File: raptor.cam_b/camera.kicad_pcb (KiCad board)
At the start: 2 copper layers, 25 x 26 mm, 7 parts

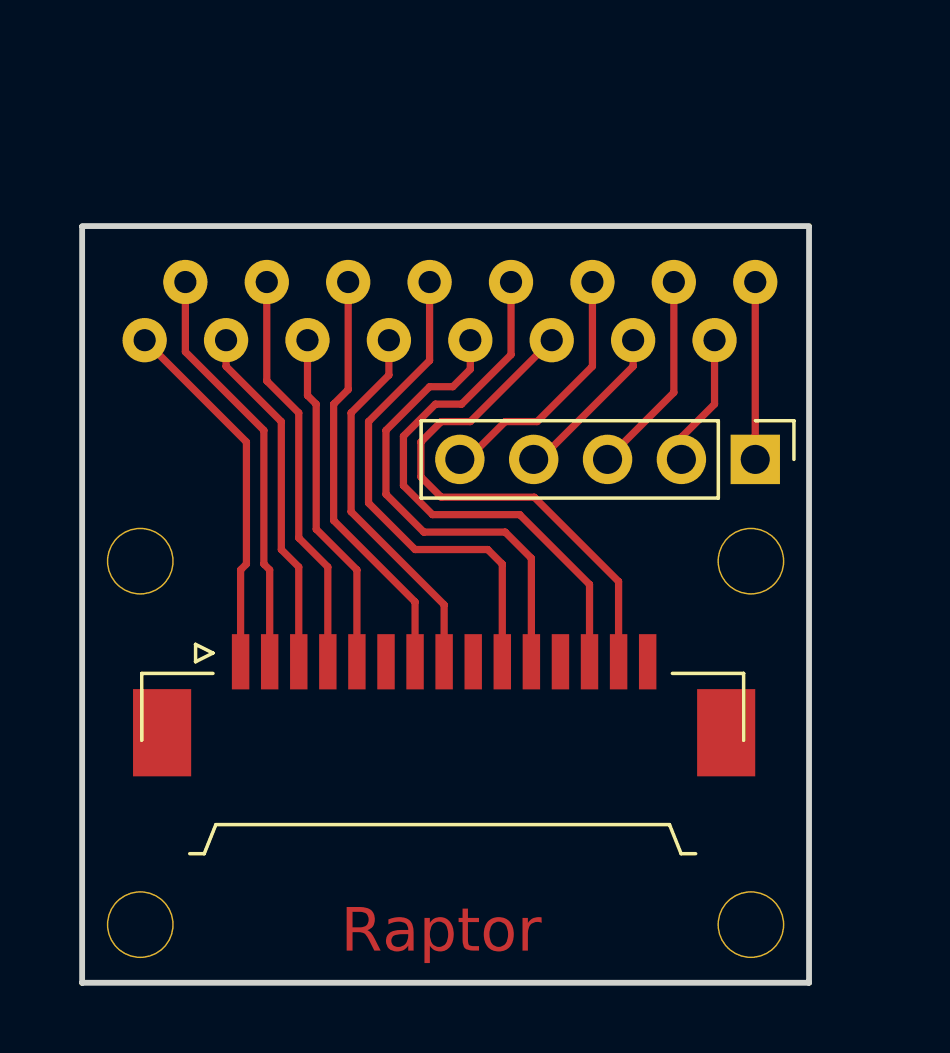
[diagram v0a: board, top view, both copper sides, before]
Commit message: Opracowałem płytkę na złącze pcb taśmy.
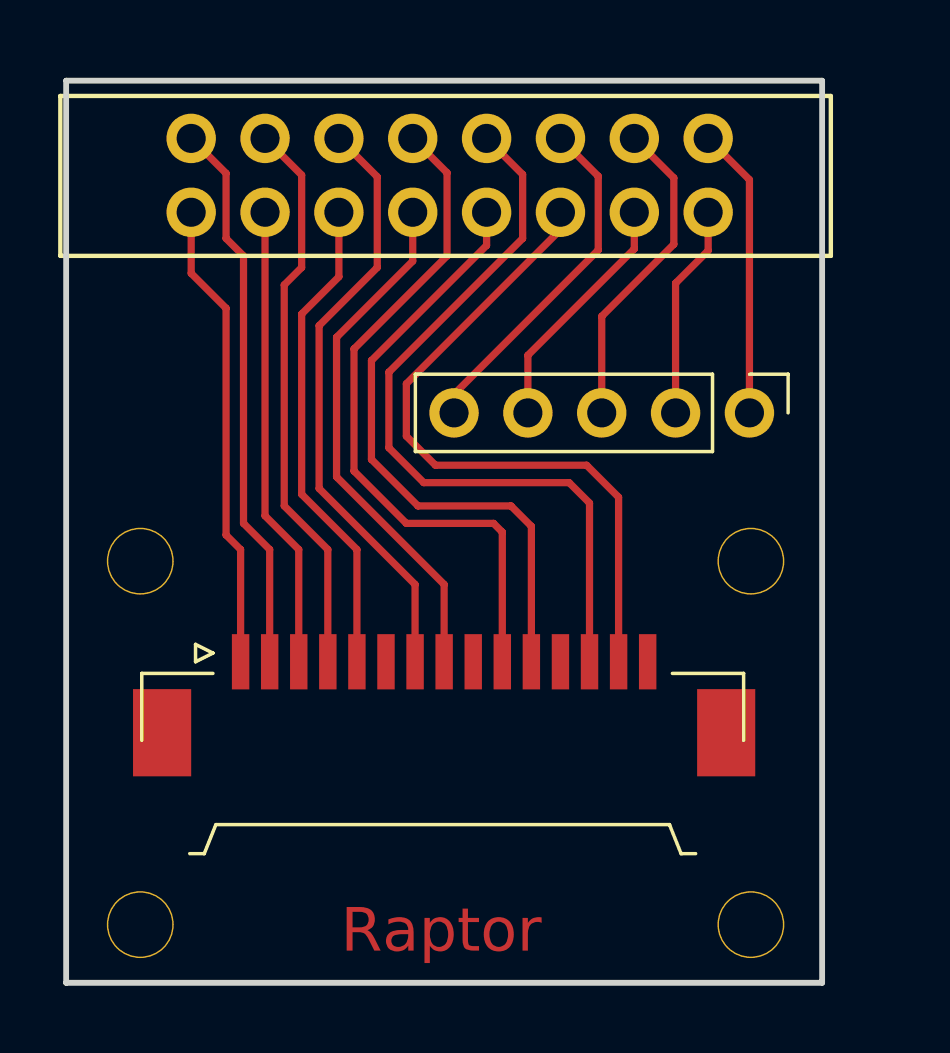
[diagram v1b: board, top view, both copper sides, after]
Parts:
- ?: footprint objects:flat_cable_connector_16pin -> objects:Przejscie_tasma_druk_2x08x2.54mm
- ?: footprint Pin_Headers:Pin_Header_Straight_1x05_Pitch2.54mm -> objects:Pin_Header_Straight_1x05_Pitch2.54mm
- moved ? 10.5 mm to (139.3, 97.5)
- moved ? 1.61 mm to (158.5, 104.4)
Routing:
- net Net-(P1-Pad13): track 19.5 -> 26.2 mm
- net Net-(P1-Pad10): track 17.3 -> 23.7 mm
- net Net-(P1-Pad7): track 14.4 -> 20.7 mm
- net Net-(P1-Pad14): track 18.2 -> 23.7 mm
- net Net-(P1-Pad4): track 13.9 -> 19.4 mm
- net Net-(P1-Pad5): track 11.8 -> 16.8 mm
- net Net-(P1-Pad2): track 14.3 -> 19.1 mm
- net Net-(P1-Pad11): track 16.4 -> 21.3 mm
- net Net-(P1-Pad8): track 13.4 -> 18.1 mm
- net Net-(P2-Pad3): track 7.04 -> 11.0 mm
- net Net-(P2-Pad1): track 6.10 -> 10.0 mm
- net Net-(P1-Pad3): track 12.1 -> 15.9 mm
- net Net-(P1-Pad1): track 12.6 -> 16.2 mm
- net Net-(P2-Pad5): track 8.83 -> 12.0 mm
- net Net-(P2-Pad2): track 4.57 -> 7.36 mm
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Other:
- board size 25 x 26 mm -> 26 x 31 mm

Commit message: Jeszcze poprawka płytki.
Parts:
- moved ? 2.90 mm to (139.3, 100.4)
- moved ? 1.71 mm to (158.3, 106.1)
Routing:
- net Net-(P1-Pad13): track 26.2 -> 22.5 mm
- net Net-(P1-Pad14): track 23.7 -> 20.1 mm
- net Net-(P1-Pad5): track 16.8 -> 13.2 mm
- net Net-(P1-Pad7): track 20.7 -> 17.2 mm
- net Net-(P1-Pad10): track 23.7 -> 20.2 mm
- net Net-(P1-Pad8): track 18.1 -> 14.7 mm
- net Net-(P1-Pad4): track 19.4 -> 16.0 mm
- net Net-(P1-Pad11): track 21.3 -> 18.0 mm
- net Net-(P1-Pad3): track 15.9 -> 13.0 mm
- net Net-(P1-Pad2): track 19.1 -> 16.5 mm
- net Net-(P1-Pad1): track 16.2 -> 14.0 mm
- net Net-(P2-Pad1): track 10.0 -> 8.75 mm
- net Net-(P2-Pad4): track 8.42 -> 7.30 mm
- net Net-(P2-Pad3): track 11.0 -> 9.91 mm
- net Net-(P2-Pad2): track 7.36 -> 6.25 mm
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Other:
- board size 26 x 31 mm -> 26 x 29 mm

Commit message: Prace nad płytką cd.
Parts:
- removed the ? at (158.3, 106.1)
- added ?: , Pin_Headers:Pin_Header_Straight_1x05_Pitch2.54mm, F.Cu at (161.2, 94.4)
- moved ? 3.06 mm to (141.2, 102.8)
- moved ? 0.45 mm to (148.1, 115.0)
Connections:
- ? pad 1: Net-(P1-Pad1) -> Net-(P1-Pad4)
- ? pad 10: Net-(P1-Pad13) -> Net-(P2-Pad4)
- ? pad 11: Net-(P1-Pad14) -> Net-(P1-Pad11)
- ? pad 13: Net-(P2-Pad4) -> Net-(P1-Pad13)
- ? pad 15: Net-(P2-Pad2) (its old number) -> Net-(P1-Pad14)
- ? pad 2: Net-(P1-Pad2) -> Net-(P1-Pad3)
- ? pad 3: Net-(P1-Pad3) -> Net-(P1-Pad5)
- ? pad 4: Net-(P1-Pad4) -> Net-(P1-Pad2)
- ? pad 5: Net-(P1-Pad5) -> Net-(P1-Pad7)
- ? pad 6: Net-(P1-Pad7) -> Net-(P1-Pad1)
- ? pad 8: Net-(P1-Pad10) -> Net-(P2-Pad5)
- ? pad 9: Net-(P1-Pad11) -> Net-(P1-Pad10)
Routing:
- net Net-(P1-Pad1): track 14.0 -> 27.9 mm
- net Net-(P1-Pad13): track 22.5 -> 11.1 mm
- net Net-(P1-Pad10): track 20.2 -> 10.2 mm
- net Net-(P1-Pad14): track 20.1 -> 11.7 mm
- net Net-(P1-Pad11): track 18.0 -> 10.9 mm
- net Net-(P1-Pad7): track 17.2 -> 10.1 mm
- net Net-(P2-Pad5): track 0.00 -> 6.78 mm
- net Net-(P2-Pad2) (its old number): track 6.25 -> 0.00 mm
- net Net-(P1-Pad2): track 16.5 -> 22.2 mm
- net Net-(P1-Pad4): track 16.0 -> 11.0 mm
- net Net-(P1-Pad8): track 14.7 -> 10.0 mm
- net Net-(P2-Pad3): track 11.0 -> 6.78 mm
- net Net-(P2-Pad2): track 9.91 -> 6.78 mm
- net Net-(P1-Pad5): track 13.2 -> 10.4 mm
- net Net-(P1-Pad3): track 13.0 -> 15.7 mm
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- added copper zone on F.Cu, net (none)
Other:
- board size 26 x 29 mm -> 28 x 32 mm
- net class Default: clearance 0.2 -> 0.4; trace_width 0.25 -> 0.45
- rule trace_clearance: 0.2 -> 0.4
